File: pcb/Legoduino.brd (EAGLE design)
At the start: 80 x 80 mm, 91 parts, among them CON11 ISP-AVR, CON2 PIN(1+16)X3_DS, IC1 NCP3170ADR2G, IC2 RN-42, IC3 MIC5205-5.0YM5, IC4 ATMEGA2560-16AU, IC5 UG-2864HSWEG01_SPI, IC6 MIC5205-3.6YM5, IC7 MIC5205-3.3YM5, IC8 BD6221F-E2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

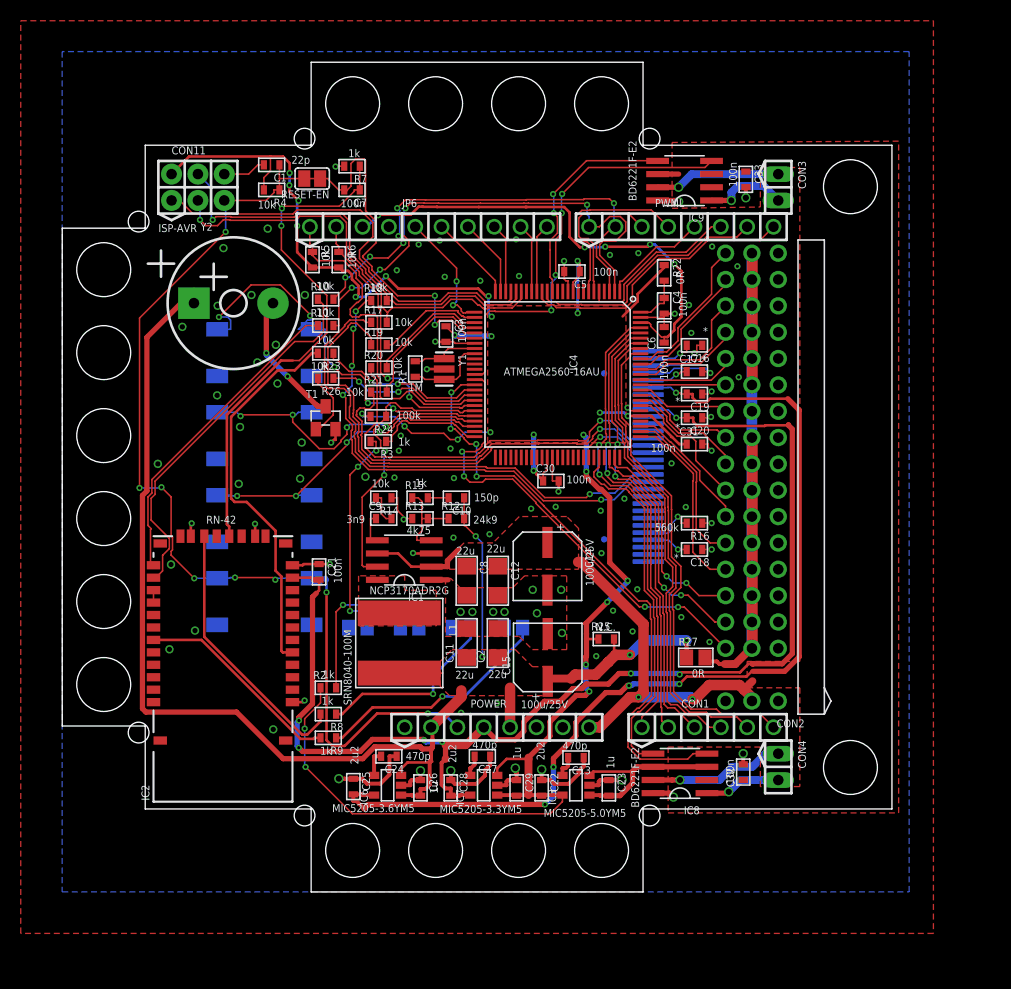
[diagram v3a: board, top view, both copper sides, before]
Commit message: Removed traces and planes from bluetooth module antenna. Closes #1
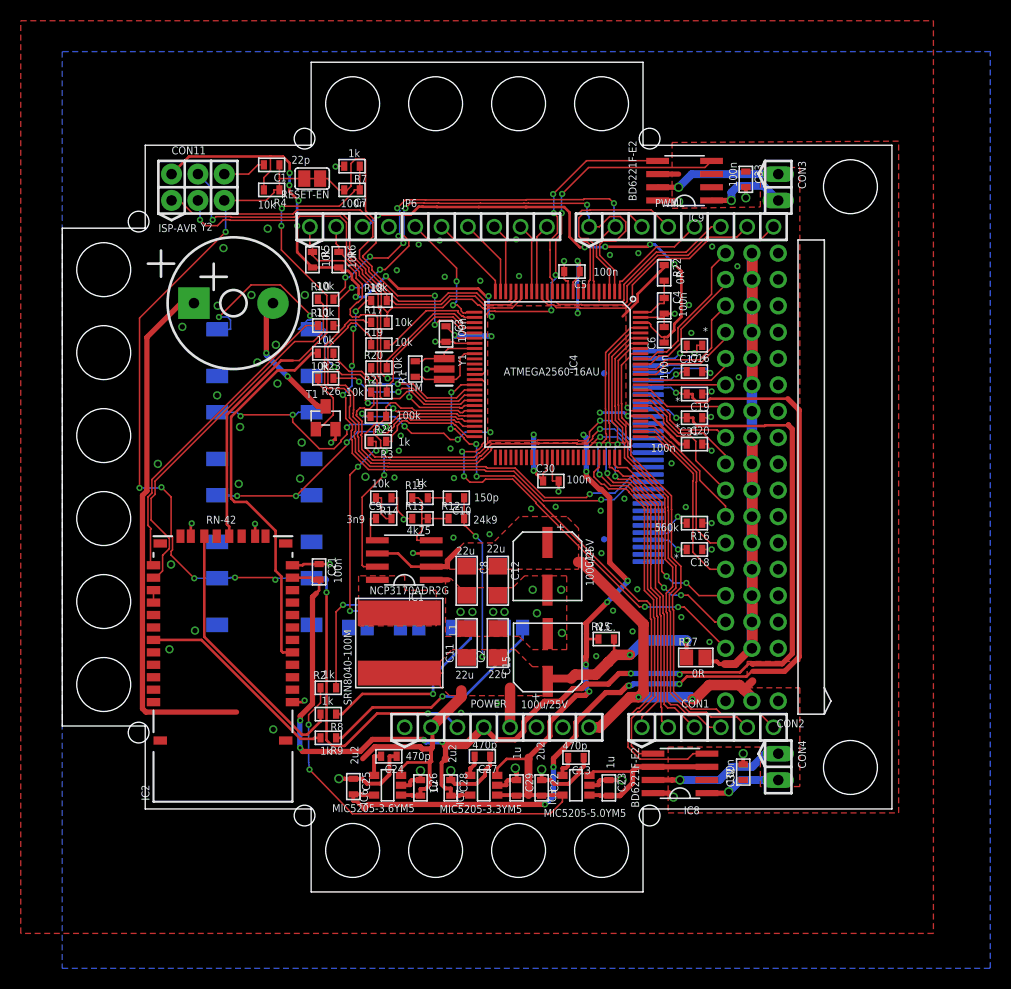
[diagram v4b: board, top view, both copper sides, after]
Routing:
- net +5VP: track 134.4 -> 120.4 mm

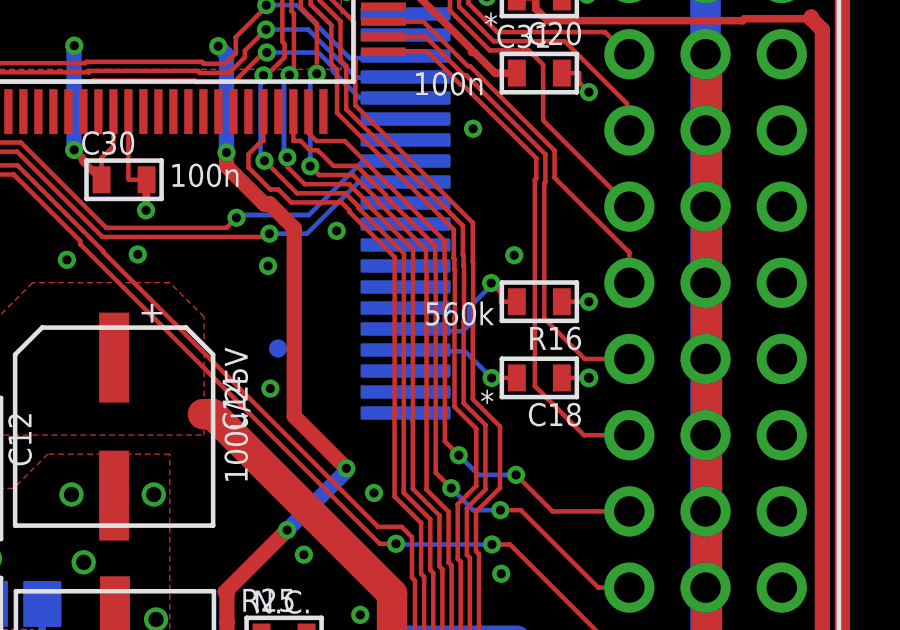
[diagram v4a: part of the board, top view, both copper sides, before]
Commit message: R16 -> 390k. Closes #32.
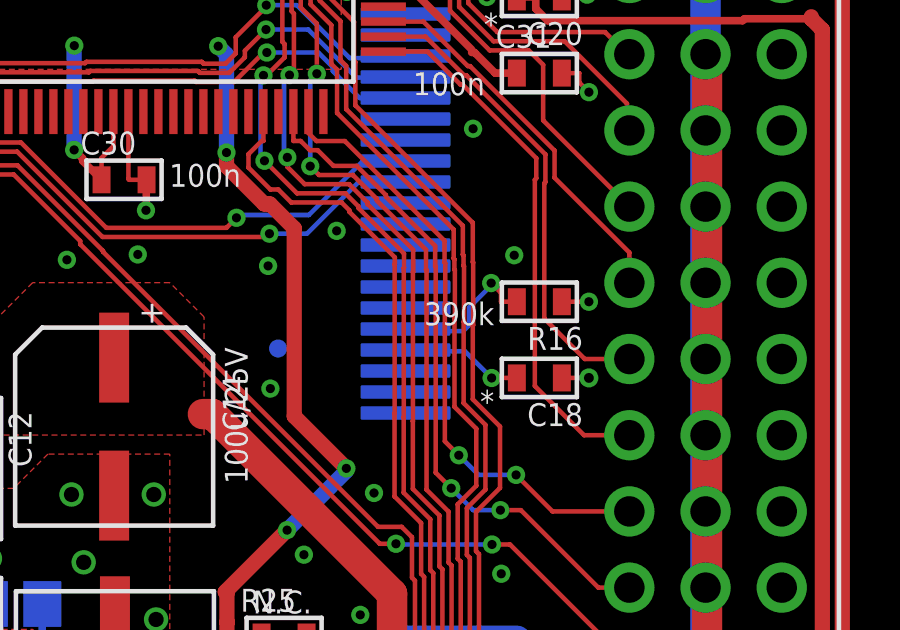
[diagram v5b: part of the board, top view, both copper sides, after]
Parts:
- R16: value 560k -> 390k
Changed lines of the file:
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@@
 <attribute name="VALUE" x="59.456" y="32.617" size="0.762" layer="100" font="vector" ratio="20" rot="R180"/>
 </element>
-<element name="R16" library="PN_default" package="0603" value="560k" x="60.96" y="35.56" smashed="yes" rot="R180">
+<element name="R16" library="PN_default" package="0603" value="390k" x="60.96" y="35.56" smashed="yes" rot="R180">
 <attribute name="NAME" x="62.411" y="34.717" size="0.762" layer="25" font="vector" ratio="20" rot="R180"/>
 <attribute name="VALUE" x="59.456" y="35.538" size="0.762" layer="100" font="vector" ratio="20" rot="R180"/>

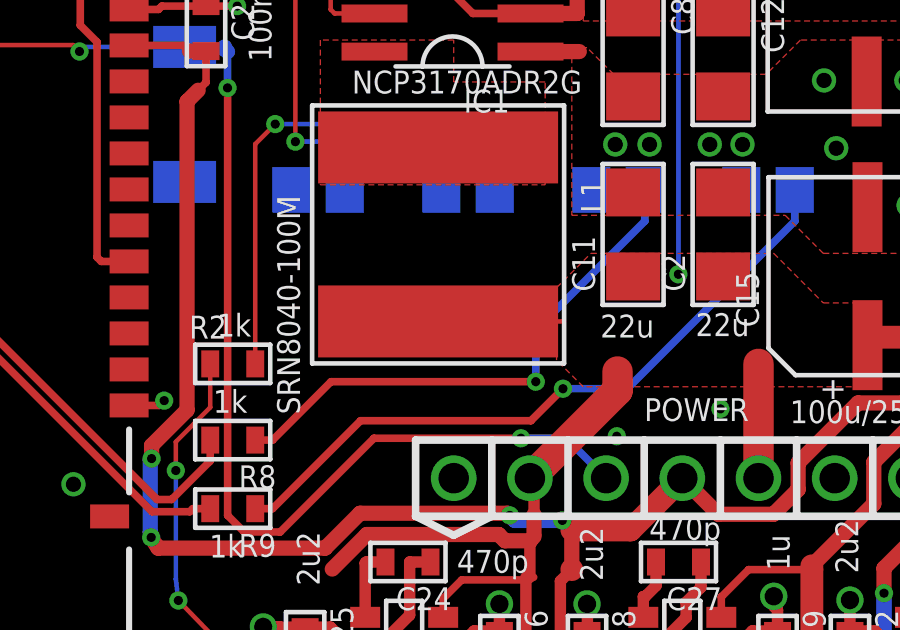
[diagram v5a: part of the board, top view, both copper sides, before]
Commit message: Reverse DATA LED polarisation. Closes #15.
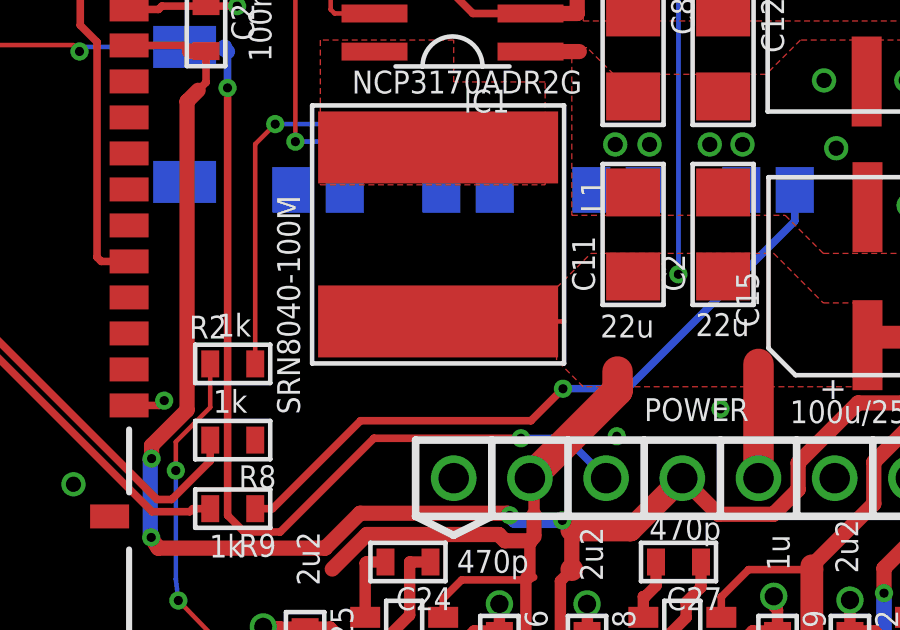
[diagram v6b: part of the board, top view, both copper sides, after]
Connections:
- net +3V3: now also D4.A
- net GND: no longer D4.K
- net N$6: now also D4.K; no longer D4.A
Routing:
- net N$6: track 18.1 -> 0.00 mm, vias 1 -> 0

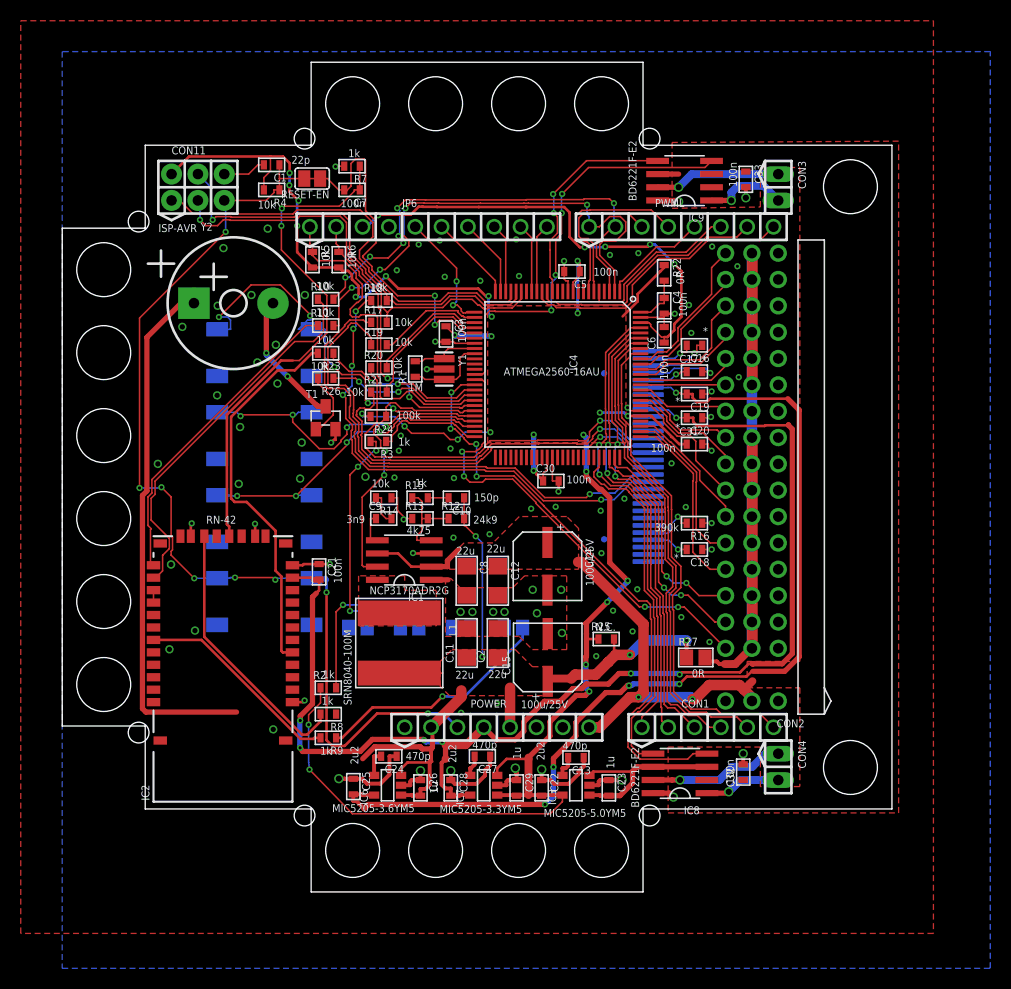
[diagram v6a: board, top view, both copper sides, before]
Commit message: #20: Optimized pin assignment on arduino shield connector. PWM signals are now connected only to this lines, where PWM are on Arduino Uno board. 4 additional PWM are now connected to expansion connector. 2 are reserved to connect to OC transistors.
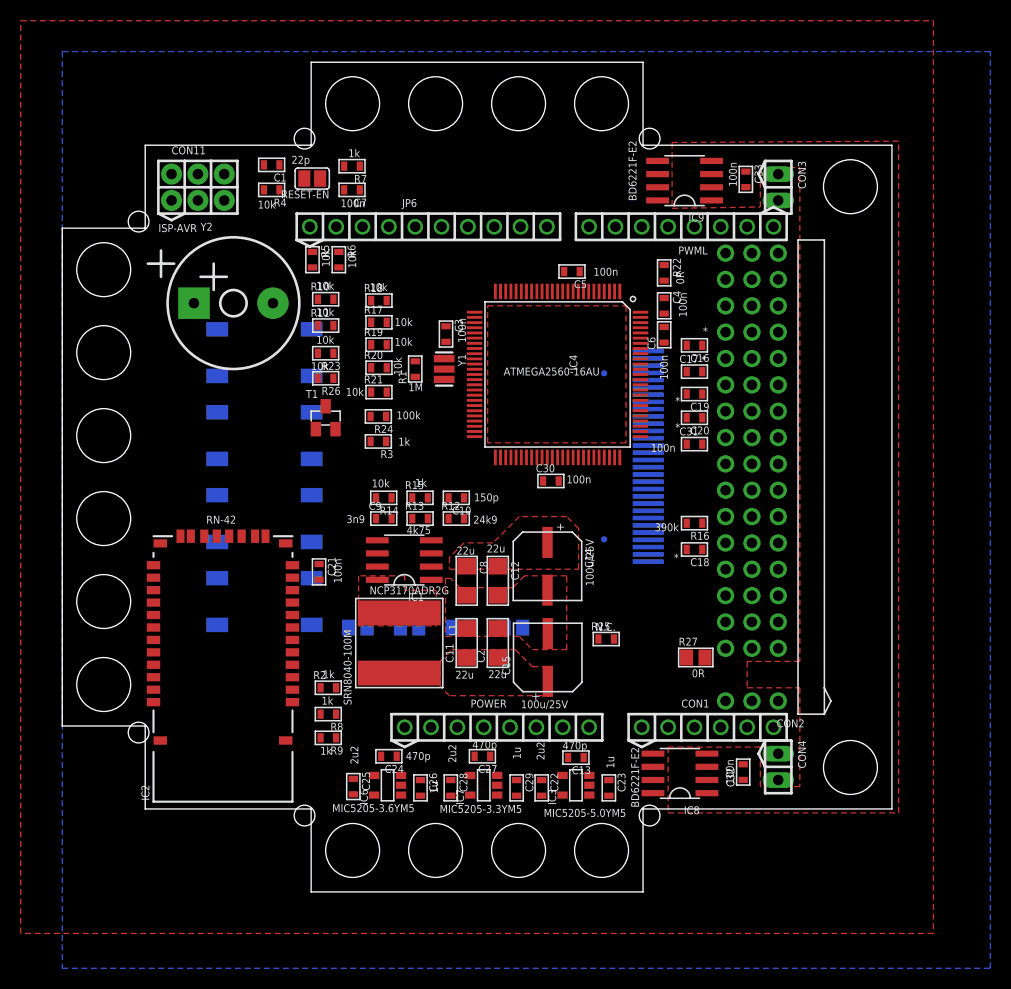
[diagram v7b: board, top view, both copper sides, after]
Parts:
- turned PWML to 180 degrees
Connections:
- removed net 45: CON2.6, IC4.39
- new net 25: CON2.15, IC4.5
- new net 28: CON2.6, IC4.38
- new net OC_PWM1: IC4.15
- new net OC_PWM2: IC4.39
- net 10: now also IC4.25; no longer IC4.23
- net 11: now also IC4.26; no longer IC4.24
- net 12: no longer IC4.25
- net 13: no longer IC4.26
- net 2: now also IC4.12; no longer IC4.6
- net 22: no longer CON2.21
- net 23: now also CON2.21; no longer CON2.18
- net 24: now also CON2.18, IC4.1; no longer CON2.15, IC4.76
- net 26: now also IC4.6; no longer IC4.74
- net 27: now also IC4.7; no longer IC4.73
- net 3: now also IC4.16; no longer IC4.7
- net 4: now also IC4.13; no longer IC4.1
- net 46: now also IC4.23; no longer IC4.38
- net 5: now also IC4.17; no longer IC4.5
- net 6: now also IC4.18; no longer IC4.15
- net 7: now also IC4.14; no longer IC4.16
- net 71: now also IC4.19; no longer IC4.14
- net 8: no longer IC4.17
- net 9: now also IC4.24; no longer IC4.18
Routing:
- net +5V: track 192.8 -> 0.00 mm, vias 28 -> 0
- net RESET: track 132.9 -> 0.00 mm, vias 10 -> 0
- net +5VP: track 120.4 -> 0.00 mm, vias 4 -> 0
- net +3V3: track 118.0 -> 0.00 mm, vias 7 -> 0
- net +3V6: track 95.5 -> 0.00 mm, vias 5 -> 0
- net GND: track 83.0 -> 0.00 mm, vias 93 -> 0
- net +5VP_O: track 76.8 -> 0.00 mm
- net VIN: track 64.6 -> 0.00 mm, vias 2 -> 0
- net 44: track 57.6 -> 0.00 mm, vias 4 -> 0
- net N$20: track 49.7 -> 0.00 mm, vias 1 -> 0
- net N$19: track 49.7 -> 0.00 mm, vias 1 -> 0
- net DTR: track 49.2 -> 0.00 mm, vias 2 -> 0
- net N$21: track 48.7 -> 0.00 mm, vias 5 -> 0
- net 1: track 47.8 -> 0.00 mm, vias 5 -> 0
- net ADC5: track 47.7 -> 0.00 mm
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
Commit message: #20: Optimized pin assignment and component placement
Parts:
- moved R9 44.0 mm to (34.5, 57.9), turned to 90 degrees
- moved R8 41.3 mm to (32.0, 57.9), turned to 90 degrees
- moved R2 38.4 mm to (29.2, 57.9), turned to 270 degrees
- moved R18 38.1 mm to (61.0, 34.0)
- moved R17 35.8 mm to (61.0, 36.1)
- moved R19 33.8 mm to (61.0, 38.1)
- moved D3 32.2 mm to (43.5, 54.0)
- moved R20 31.6 mm to (61.0, 42.2)
- moved R21 31.5 mm to (61.0, 40.1)
- moved D2 29.0 mm to (28.5, 54.0)
- moved D4 29.0 mm to (33.5, 54.0)
- moved D5 29.0 mm to (38.5, 54.0)
- moved R3 15.9 mm to (37.1, 57.9), turned to 270 degrees
- moved T1 5.47 mm to (20.3, 47.8)
- moved IC5 4.00 mm to (33.5, 38.0)
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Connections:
- net 12: now also IC4.28
- net 13: now also IC4.29
- net 38: now also IC4.37; no longer IC4.50
- net 70: no longer IC4.27
- net 72: no longer IC4.28
- net 73: no longer IC4.29
- net 8: now also IC4.27
- net ADC0: now also IC4.89; no longer IC4.97
- net ADC1: now also IC4.88; no longer IC4.96
- net ADC10: now also CON2.45, IC4.95; no longer CON2.39, IC4.87
- net ADC11: now also CON2.42, IC4.94; no longer CON2.36, IC4.86
- net ADC12: now also CON2.39, IC4.93; no longer CON2.33, IC4.85
- net ADC13: now also CON2.36, IC4.92; no longer CON2.30, IC4.84
- net ADC14: now also CON2.33, IC4.91; no longer CON2.27, IC4.83
- net ADC15: now also CON2.30, IC4.90; no longer CON2.24, IC4.82
- net ADC2: now also IC4.87; no longer IC4.95
- net ADC3: now also IC4.86; no longer IC4.94
- net ADC4: now also IC4.85; no longer IC4.93
- net ADC5: now also IC4.84; no longer IC4.92
- net ADC6: now also CON2.27, IC4.83; no longer CON2.51, IC4.91
- net ADC7: now also CON2.24, IC4.82; no longer CON2.48, IC4.90
- net ADC8: now also CON2.51, IC4.97; no longer CON2.45, IC4.89
- net ADC9: now also CON2.48, IC4.96; no longer CON2.42, IC4.88
